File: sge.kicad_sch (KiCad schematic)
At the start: 27 parts, among them IC6 315-5660

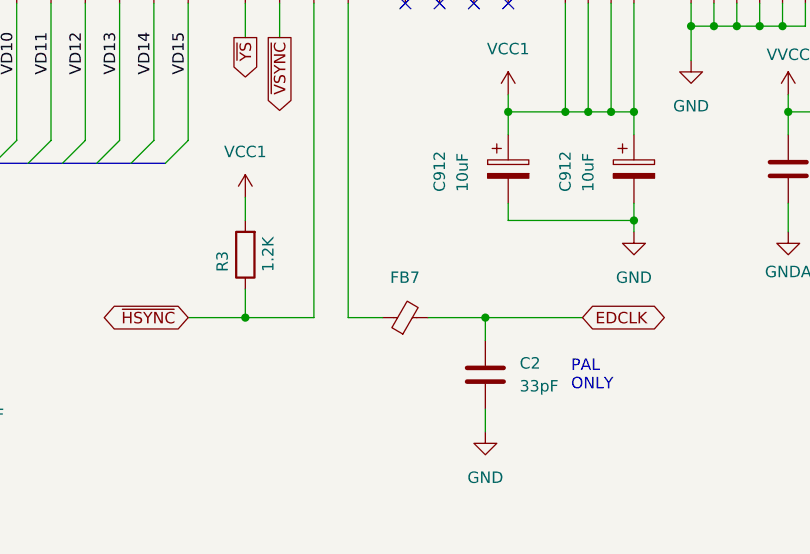
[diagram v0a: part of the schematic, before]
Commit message: Ferrite Bead LCSC Part update
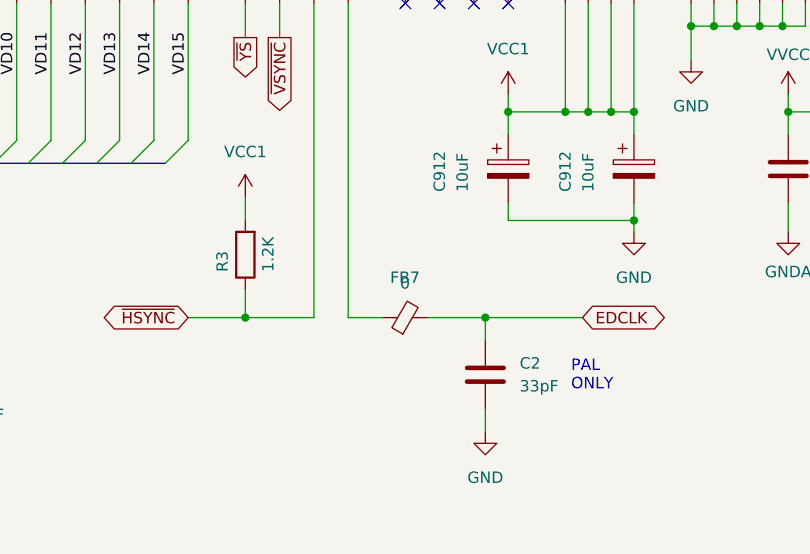
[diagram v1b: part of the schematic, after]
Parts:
- FB7: value ~ -> 0; LCSC Part # C2441367 -> C91037
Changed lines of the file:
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@@
       (effects (font (size 1.27 1.27)))
     )
-    (property "Value" "~" (at 252.6919 250.825 90)
+    (property "Value" "0" (at 252.6919 250.825 90)
       (effects (font (size 1.27 1.27)))
     )
@@
       (effects (font (size 1.27 1.27)) hide)
     )
-    (property "LCSC Part #" "C2441367" (at 252.73 254.635 0)
+    (property "LCSC Part #" "C91037" (at 252.73 254.635 0)
       (effects (font (size 1.27 1.27)) hide)
     )

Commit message: more component parts updated
Full in the * as PAL versions.
Added MPN for PCBWAY
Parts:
- C1: MPN (none) -> VJ0805Y223JXJPW1BC
- C1: MPN (none) -> VJ0805A470FXJPW1BC
- C2: MPN (none) -> VJ0805A330FXJPW1BC
- C8: MPN (none) -> VJ0805Y105KXJTW1BC
- FB7: MPN (none) -> CBG201209U000T
- R3: MPN (none) -> CRCW08052K20JNEA
- R3: MPN (none) -> CRCW08054K70JNEAC
- R3: MPN (none) -> CRCW08051K20FKEAHP
- RA1, RA2, RA3, RA4, RA5: MPN (none) -> YC164-FR-07100RL
- RA6: MPN (none) -> YC162-FR-07100RL
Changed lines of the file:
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@@
+      (effects (font (size 1.27 1.27)) hide)
+    )
+    (property "MPN" "YC164-FR-07100RL" (at 113.03 38.1 0)
       (effects (font (size 1.27 1.27)) hide)
     )
@@
     )
     (property "LCSC Part #" "" (at 213.36 130.81 0)
+      (effects (font (size 1.27 1.27)) hide)
+    )
+    (property "MPN" "" (at 213.36 130.81 0)
       (effects (font (size 1.27 1.27)) hide)
     )
@@
       (effects (font (size 1.27 1.27)) hide)
     )
+    (property "MPN" "CRCW08052K20JNEA" (at 139.7 256.54 0)
+      (effects (font (size 1.27 1.27)) hide)
+    )
     (pin "1")
     (pin "2")
@@
     )
     (property "LCSC Part #" "C136838" (at 99.06 38.1 0)
+      (effects (font (size 1.27 1.27)) hide)
+    )
+    (property "MPN" "YC164-FR-07100RL" (at 99.06 38.1 0)
       (effects (font (size 1.27 1.27)) hide)
     )
@@
       (effects (font (size 1.27 1.27)) hide)
     )
+    (property "MPN" "YC164-FR-07100RL" (at 124.46 38.1 0)
+      (effects (font (size 1.27 1.27)) hide)
+    )
     (pin "1")
     (pin "8")
@@
       (effects (font (size 1.27 1.27)) hide)
     )
+    (property "MPN" "YC164-FR-07100RL" (at 116.84 38.1 0)
+      (effects (font (size 1.27 1.27)) hide)
+    )
     (pin "1")
     (pin "8")
@@
       (effects (font (size 1.27 1.27)) hide)
     )
+    (property "MPN" "" (at 264.16 238.125 0)
+      (effects (font (size 1.27 1.27)) hide)
+    )
     (pin "1")
     (pin "2")
@@
     )
     (property "LCSC Part #" "C136838" (at 198.12 38.1 0)
+      (effects (font (size 1.27 1.27)) hide)
+    )
+    (property "MPN" "YC164-FR-07100RL" (at 198.12 38.1 0)
       (effects (font (size 1.27 1.27)) hide)
     )
@@
       (effects (font (size 1.27 1.27)) hide)
     )
+    (property "MPN" "VJ0805A330FXJPW1BC" (at 261.62 260.985 0)
+      (effects (font (size 1.27 1.27)) hide)
+    )
     (pin "1")
     (pin "2")
@@
       (effects (font (size 1.27 1.27)) hide)
     )
+    (property "MPN" "YC162-FR-07100RL" (at 106.68 38.1 0)
+      (effects (font (size 1.27 1.27)) hide)
+    )
     (pin "1")
     (pin "4")
@@
       (effects (font (size 1.27 1.27)) hide)
     )
+    (property "MPN" "CRCW08052K20JNEA" (at 392.43 52.07 0)
+      (effects (font (size 1.27 1.27)) hide)
+    )
     (pin "1")
     (pin "2")
@@
       (effects (font (size 1.27 1.27)) hide)
     )
+    (property "MPN" "VJ0805Y223JXJPW1BC" (at 175.26 264.16 0)
+      (effects (font (size 1.27 1.27)) hide)
+    )
     (pin "1")
     (pin "2")
@@
       (effects (font (size 1.27 1.27)) hide)
     )
+    (property "MPN" "VJ0805Y105KXJTW1BC" (at 30.48 174.625 0)
+      (effects (font (size 1.27 1.27)) hide)
+    )
     (pin "1")
     (pin "2")
@@
       (effects (font (size 1.27 1.27)) hide)
     )
+    (property "MPN" "VJ0805Y223JXJPW1BC" (at 160.655 264.16 0)
+      (effects (font (size 1.27 1.27)) hide)
+    )
     (pin "1")
     (pin "2")
@@
       (effects (font (size 1.27 1.27)) hide)
     )
+    (property "MPN" "VJ0805Y223JXJPW1BC" (at 295.275 238.125 0)
+      (effects (font (size 1.27 1.27)) hide)
+    )
     (pin "1")
     (pin "2")
@@
     )
     (property "LCSC Part #" "C136838" (at 135.89 38.1 0)
+      (effects (font (size 1.27 1.27)) hide)
+    )
+    (property "MPN" "YC164-FR-07100RL" (at 135.89 38.1 0)
       (effects (font (size 1.27 1.27)) hide)
     )
@@
       (effects (font (size 1.27 1.27)) hide)
     )
+    (property "MPN" "YC162-FR-07100RL" (at 83.82 38.1 0)
+      (effects (font (size 1.27 1.27)) hide)
+    )
     (pin "1")
     (pin "4")
@@
     )
     (property "LCSC Part #" "C136838" (at 120.65 38.1 0)
+      (effects (font (size 1.27 1.27)) hide)
+    )
+    (property "MPN" "YC164-FR-07100RL" (at 120.65 38.1 0)
       (effects (font (size 1.27 1.27)) hide)
     )
@@
       (effects (font (size 1.27 1.27)) hide)
     )
+    (property "MPN" "YC164-FR-07100RL" (at 179.07 38.1 0)
+      (effects (font (size 1.27 1.27)) hide)
+    )
     (pin "1")
     (pin "8")
@@
       (effects (font (size 1.27 1.27)) hide)
     )
+    (property "MPN" "CRCW08052K20JNEA" (at 354.33 229.87 0)
+      (effects (font (size 1.27 1.27)) hide)
+    )
     (pin "1")
     (pin "2")
@@
     )
     (property "LCSC Part #" "C136838" (at 132.08 38.1 0)
+      (effects (font (size 1.27 1.27)) hide)
+    )
+    (property "MPN" "YC164-FR-07100RL" (at 132.08 38.1 0)
       (effects (font (size 1.27 1.27)) hide)
     )
@@
       (effects (font (size 1.27 1.27)) hide)
     )
+    (property "MPN" "" (at 127 256.54 0)
+      (effects (font (size 1.27 1.27)) hide)
+    )
     (pin "1")
     (pin "2")
@@
     )
     (property "LCSC Part #" "C136838" (at 201.93 38.1 0)
+      (effects (font (size 1.27 1.27)) hide)
+    )
+    (property "MPN" "YC164-FR-07100RL" (at 201.93 38.1 0)
       (effects (font (size 1.27 1.27)) hide)
     )
@@
       (effects (font (size 1.27 1.27)) hide)
     )
+    (property "MPN" "VJ0805Y223JXJPW1BC" (at 321.31 238.125 0)
+      (effects (font (size 1.27 1.27)) hide)
+    )
     (pin "1")
     (pin "2")
@@
     )
     (property "LCSC Part #" "C136838" (at 194.31 38.1 0)
+      (effects (font (size 1.27 1.27)) hide)
+    )
+    (property "MPN" "YC164-FR-07100RL" (at 194.31 38.1 0)
       (effects (font (size 1.27 1.27)) hide)
     )
@@
       (effects (font (size 1.27 1.27)) hide)
     )
+    (property "MPN" "YC164-FR-07100RL" (at 128.27 38.1 0)
+      (effects (font (size 1.27 1.27)) hide)
+    )
     (pin "1")
     (pin "8")
@@
       (effects (font (size 1.27 1.27)) hide)
     )
+    (property "MPN" "YC164-FR-07100RL" (at 102.87 38.1 0)
+      (effects (font (size 1.27 1.27)) hide)
+    )
     (pin "1")
     (pin "8")
@@
       (effects (font (size 1.27 1.27)) hide)
     )
+    (property "MPN" "CRCW08054K70JNEAC" (at 390.525 195.58 0)
+      (effects (font (size 1.27 1.27)) hide)
+    )
     (pin "1")
     (pin "2")
@@
       (effects (font (size 1.27 1.27)) hide)
     )
+    (property "MPN" "VJ0805Y223JXJPW1BC" (at 314.96 238.125 0)
+      (effects (font (size 1.27 1.27)) hide)
+    )
     (pin "1")
     (pin "2")
@@
     )
     (property "LCSC Part #" "C136838" (at 80.01 38.1 0)
+      (effects (font (size 1.27 1.27)) hide)
+    )
+    (property "MPN" "YC164-FR-07100RL" (at 80.01 38.1 0)
       (effects (font (size 1.27 1.27)) hide)
     )
@@
       (effects (font (size 1.27 1.27)) hide)
     )
+    (property "MPN" "CBG201209U000T" (at 252.73 254.635 0)
+      (effects (font (size 1.27 1.27)) hide)
+    )
     (pin "1")
     (pin "2")
@@
     )
     (property "LCSC Part #" "C136838" (at 190.5 38.1 0)
+      (effects (font (size 1.27 1.27)) hide)
+    )
+    (property "MPN" "YC164-FR-07100RL" (at 190.5 38.1 0)
       (effects (font (size 1.27 1.27)) hide)
     )
@@
       (effects (font (size 1.27 1.27)) hide)
     )
+    (property "MPN" "YC164-FR-07100RL" (at 139.7 38.1 0)
+      (effects (font (size 1.27 1.27)) hide)
+    )
     (pin "1")
     (pin "8")
@@
       (effects (font (size 1.27 1.27)) hide)
     )
+    (property "MPN" "CRCW08051K20FKEAHP" (at 234.95 247.65 0)
+      (effects (font (size 1.27 1.27)) hide)
+    )
     (pin "1")
     (pin "2")
@@
       (effects (font (size 1.27 1.27)) hide)
     )
+    (property "MPN" "" (at 278.13 238.125 0)
+      (effects (font (size 1.27 1.27)) hide)
+    )
     (pin "1")
     (pin "2")
@@
     )
     (property "LCSC Part #" "C136838" (at 205.74 38.1 0)
+      (effects (font (size 1.27 1.27)) hide)
+    )
+    (property "MPN" "YC164-FR-07100RL" (at 205.74 38.1 0)
       (effects (font (size 1.27 1.27)) hide)
     )
@@
       (effects (font (size 1.27 1.27)) hide)
     )
+    (property "MPN" "VJ0805A470FXJPW1BC" (at 388.62 72.39 0)
+      (effects (font (size 1.27 1.27)) hide)
+    )
     (pin "1")
     (pin "2")
@@
     )
     (property "LCSC Part #" "C136838" (at 95.25 38.1 0)
+      (effects (font (size 1.27 1.27)) hide)
+    )
+    (property "MPN" "YC164-FR-07100RL" (at 95.25 38.1 0)
       (effects (font (size 1.27 1.27)) hide)
     )
@@
       (effects (font (size 1.27 1.27)) hide)
     )
+    (property "MPN" "VJ0805Y105KXJTW1BC" (at 31.115 71.755 0)
+      (effects (font (size 1.27 1.27)) hide)
+    )
     (pin "1")
     (pin "2")
@@
       (effects (font (size 1.27 1.27)) hide)
     )
+    (property "MPN" "VJ0805Y223JXJPW1BC" (at 200.025 264.16 0)
+      (effects (font (size 1.27 1.27)) hide)
+    )
     (pin "1")
     (pin "2")
@@
     )
     (property "LCSC Part #" "C136838" (at 186.69 38.1 0)
+      (effects (font (size 1.27 1.27)) hide)
+    )
+    (property "MPN" "YC164-FR-07100RL" (at 186.69 38.1 0)
       (effects (font (size 1.27 1.27)) hide)
     )
@@
       (effects (font (size 1.27 1.27)) hide)
     )
+    (property "MPN" "VJ0805Y223JXJPW1BC" (at 187.96 264.16 0)
+      (effects (font (size 1.27 1.27)) hide)
+    )
     (pin "1")
     (pin "2")
@@
       (effects (font (size 1.27 1.27)) hide)
     )
+    (property "MPN" "YC164-FR-07100RL" (at 182.88 38.1 0)
+      (effects (font (size 1.27 1.27)) hide)
+    )

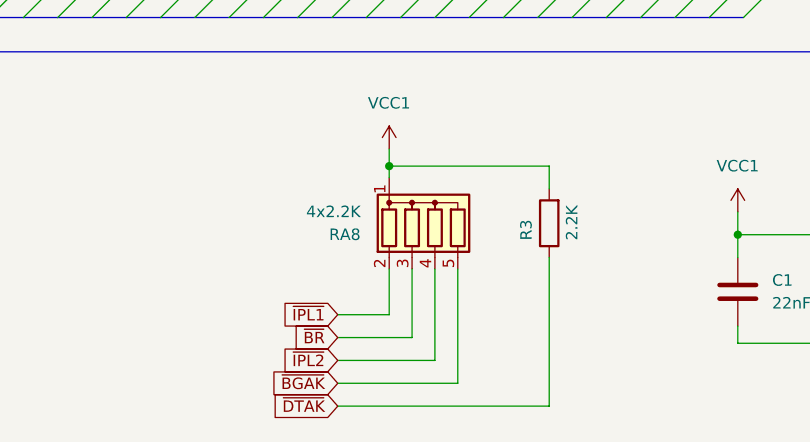
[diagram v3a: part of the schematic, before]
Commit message: Use more readily-available resistor packs.
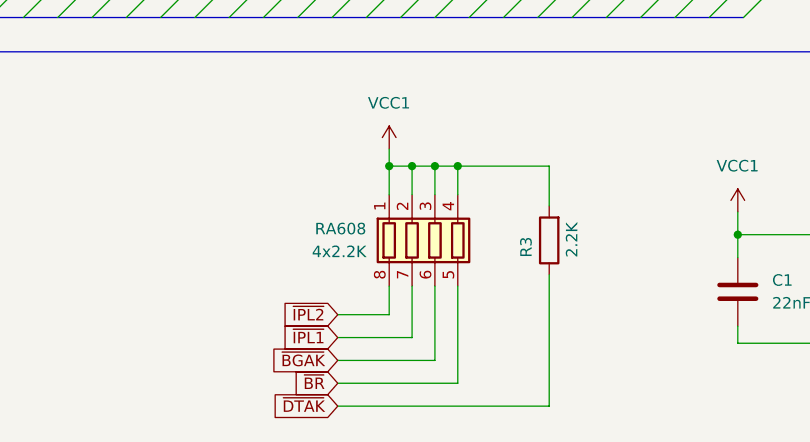
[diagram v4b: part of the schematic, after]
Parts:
- removed RA8: 4x2.2K, Neptune:RA_4_Common, symbol Device:R_Network04
- added RA608: 4x2.2K, Resistor_SMD:R_Array_Convex_4x0603, symbol Device:R_Pack04
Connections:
- net VCC1: now also RA608.1 (R1.1), RA608.2 (R2.1), RA608.3 (R3.1), RA608.4 (R4.1)
- net ~{BGAK}: now also RA608.6 (R3.2)
- net ~{BR}: now also RA608.5 (R4.2)
- net ~{IPL1}: now also RA608.7 (R2.2)
- net ~{IPL2}: now also RA608.8 (R1.2)
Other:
- moved on the sheet: R3
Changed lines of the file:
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@@
   (junction (at 292.1 222.25) (diameter 0) (color 0 0 0 0)
   )
+  (junction (at 127 250.19) (diameter 0) (color 0 0 0 0)
+  )
   (junction (at 388.62 60.96) (diameter 0) (color 0 0 0 0)
   )
@@
   (junction (at 31.115 64.77) (diameter 0) (color 0 0 0 0)
   )
+  (junction (at 129.54 250.19) (diameter 0) (color 0 0 0 0)
+  )
   (junction (at 278.13 243.84) (diameter 0) (color 0 0 0 0)
   )
@@
   (junction (at 234.95 254.635) (diameter 0) (color 0 0 0 0)
   )
+  (junction (at 124.46 250.19) (diameter 0) (color 0 0 0 0)
+  )
   (junction (at 289.56 222.25) (diameter 0) (color 0 0 0 0)
   )
@@
     (stroke (width 0) (type default))
   )
-  (wire (pts (xy 124.46 269.24) (xy 124.46 261.62))
+  (wire (pts (xy 124.46 269.24) (xy 124.46 263.525))
     (stroke (width 0) (type default))
   )
@@
     (stroke (width 0) (type default))
   )
+  (wire (pts (xy 129.54 250.19) (xy 129.54 253.365))
+    (stroke (width 0) (type default))
+  )
   (wire (pts (xy 314.96 243.84) (xy 321.31 243.84))
     (stroke (width 0) (type default))
@@
     (stroke (width 0) (type default))
   )
-  (wire (pts (xy 121.92 250.19) (xy 139.7 250.19))
+  (wire (pts (xy 121.92 250.19) (xy 124.46 250.19))
     (stroke (width 0) (type default))
   )
@@
     (stroke (width 0) (type default))
   )
+  (wire (pts (xy 127 250.19) (xy 127 253.365))
+    (stroke (width 0) (type default))
+  )
   (bus (pts (xy 299.72 24.13) (xy 295.91 24.13))
     (stroke (width 0) (type default))
@@
     (stroke (width 0) (type default))
   )
+  (wire (pts (xy 127 250.19) (xy 129.54 250.19))
+    (stroke (width 0) (type default))
+  )
   (bus (pts (xy 153.67 233.68) (xy 157.48 233.68))
     (stroke (width 0) (type default))
@@
     (stroke (width 0) (type default))
   )
-  (wire (pts (xy 121.92 250.19) (xy 121.92 251.46))
+  (wire (pts (xy 121.92 250.19) (xy 121.92 253.365))
     (stroke (width 0) (type default))
   )
@@
     (stroke (width 0) (type default))
   )
+  (wire (pts (xy 124.46 250.19) (xy 127 250.19))
+    (stroke (width 0) (type default))
+  )
   (wire (pts (xy 113.03 22.86) (xy 113.03 34.29))
     (stroke (width 0) (type default))
@@
     (stroke (width 0) (type default))
   )
-  (wire (pts (xy 129.54 274.32) (xy 129.54 261.62))
+  (wire (pts (xy 129.54 274.32) (xy 129.54 263.525))
     (stroke (width 0) (type default))
   )
@@
     (stroke (width 0) (type default))
   )
+  (wire (pts (xy 129.54 250.19) (xy 139.7 250.19))
+    (stroke (width 0) (type default))
+  )
   (wire (pts (xy 364.49 156.21) (xy 375.92 156.21))
     (stroke (width 0) (type default))
@@
     (stroke (width 0) (type default))
   )
+  (wire (pts (xy 124.46 250.19) (xy 124.46 253.365))
+    (stroke (width 0) (type default))
+  )
   (wire (pts (xy 50.8 129.54) (xy 62.23 129.54))
     (stroke (width 0) (type default))
@@
     (stroke (width 0) (type default))
   )
-  (wire (pts (xy 121.92 266.7) (xy 121.92 261.62))
+  (wire (pts (xy 121.92 266.7) (xy 121.92 263.525))
     (stroke (width 0) (type default))
   )
@@
     (stroke (width 0) (type default))
   )
-  (wire (pts (xy 127 271.78) (xy 127 261.62))
+  (wire (pts (xy 127 271.78) (xy 127 263.525))
     (stroke (width 0) (type default))
   )
@@
     (stroke (width 0) (type default))
   )
-  (wire (pts (xy 139.7 250.19) (xy 139.7 252.73))
+  (wire (pts (xy 139.7 250.19) (xy 139.7 254.635))
     (stroke (width 0) (type default))
   )
@@
     (stroke (width 0) (type default))
   )
-  (wire (pts (xy 139.7 276.86) (xy 139.7 260.35))
+  (wire (pts (xy 139.7 276.86) (xy 139.7 262.255))
     (stroke (width 0) (type default))
   )
@@
     )
   )
-  (global_label "~{IPL2}" (shape input) (at 116.205 271.78 180) (fields_autoplaced)
+  (global_label "~{IPL2}" (shape input) (at 116.205 266.7 180) (fields_autoplaced)
     (effects (font (size 1.27 1.27)) (justify right))
-    (property "Intersheetrefs" "${INTERSHEET_REFS}" (at 109.1074 271.78 0)
+    (property "Intersheetrefs" "${INTERSHEET_REFS}" (at 109.1074 266.7 0)
       (effects (font (size 1.27 1.27)) (justify right) hide)
     )
@@
     )
   )
-  (global_label "~{IPL1}" (shape input) (at 116.205 266.7 180) (fields_autoplaced)
+  (global_label "~{IPL1}" (shape input) (at 116.205 269.24 180) (fields_autoplaced)
     (effects (font (size 1.27 1.27)) (justify right))
-    (property "Intersheetrefs" "${INTERSHEET_REFS}" (at 109.1074 266.7 0)
+    (property "Intersheetrefs" "${INTERSHEET_REFS}" (at 109.1074 269.24 0)
       (effects (font (size 1.27 1.27)) (justify right) hide)
     )
@@
     )
   )
-  (global_label "~{BGAK}" (shape input) (at 116.205 274.32 180) (fields_autoplaced)
+  (global_label "~{BGAK}" (shape input) (at 116.205 271.78 180) (fields_autoplaced)
     (effects (font (size 1.27 1.27)) (justify right))
-    (property "Intersheetrefs" "${INTERSHEET_REFS}" (at 108.3212 274.32 0)
+    (property "Intersheetrefs" "${INTERSHEET_REFS}" (at 108.3212 271.78 0)
       (effects (font (size 1.27 1.27)) (justify right) hide)
     )
@@
     )
   )
-  (global_label "~{BR}" (shape input) (at 116.205 269.24 180) (fields_autoplaced)
+  (global_label "~{BR}" (shape input) (at 116.205 274.32 180) (fields_autoplaced)
     (effects (font (size 1.27 1.27)) (justify right))
-    (property "Intersheetrefs" "${INTERSHEET_REFS}" (at 110.6798 269.24 0)
+    (property "Intersheetrefs" "${INTERSHEET_REFS}" (at 110.6798 274.32 0)
       (effects (font (size 1.27 1.27)) (justify right) hide)
     )
@@
     )
   )
-  (symbol (lib_id "Device:R") (at 139.7 256.54 180) (unit 1)
+  (symbol (lib_id "Device:R") (at 139.7 258.445 180) (unit 1)
     (in_bom yes) (on_board yes) (dnp no)
-    (property "Reference" "R3" (at 137.16 258.445 90)
+    (property "Reference" "R3" (at 137.16 260.35 90)
       (effects (font (size 1.27 1.27)) (justify right))
     )
-    (property "Value" "2.2K" (at 142.24 258.445 90)
+    (property "Value" "2.2K" (at 142.24 260.35 90)
       (effects (font (size 1.27 1.27)) (justify right))
     )
-    (property "Footprint" "Resistor_SMD:R_0805_2012Metric" (at 141.478 256.54 90)
+    (property "Footprint" "Resistor_SMD:R_0805_2012Metric" (at 141.478 258.445 90)
       (effects (font (size 1.27 1.27)) hide)
     )
-    (property "Datasheet" "~" (at 139.7 256.54 0)
+    (property "Datasheet" "~" (at 139.7 258.445 0)
       (effects (font (size 1.27 1.27)) hide)
     )
-    (property "DigiKey" "P2.20KCCT-ND" (at 139.7 256.54 0)
+    (property "DigiKey" "P2.20KCCT-ND" (at 139.7 258.445 0)
       (effects (font (size 1.27 1.27)) hide)
     )
-    (property "LCSC Part #" "C3008897" (at 139.7 256.54 0)
+    (property "LCSC Part #" "C3008897" (at 139.7 258.445 0)
       (effects (font (size 1.27 1.27)) hide)
     )
-    (property "MPN" "CRCW08052K20JNEA" (at 139.7 256.54 0)
+    (property "MPN" "CRCW08052K20JNEA" (at 139.7 258.445 0)
       (effects (font (size 1.27 1.27)) hide)
     )
@@
     )
   )
-  (symbol (lib_id "Device:R_Network04") (at 127 256.54 0) (unit 1)
-    (in_bom yes) (on_board yes) (dnp no)
-    (property "Reference" "RA8" (at 118.745 257.81 0)
-      (effects (font (size 1.27 1.27)) (justify right))
-    )
-    (property "Value" "4x2.2K" (at 118.745 255.27 0)
-      (effects (font (size 1.27 1.27)) (justify right))
-    )
-    (property "Footprint" "Neptune:RA_4_Common" (at 133.985 256.54 90)
-      (effects (font (size 1.27 1.27)) hide)
-    )
-    (property "Datasheet" "http://www.vishay.com/docs/31509/csc.pdf" (at 127 256.54 0)
-      (effects (font (size 1.27 1.27)) hide)
-    )
-    (property "DigiKey" "" (at 127 256.54 0)
-      (effects (font (size 1.27 1.27)) hide)
-    )
-    (property "LCSC Part #" "" (at 127 256.54 0)
-      (effects (font (size 1.27 1.27)) hide)
-    )
-    (property "MPN" "" (at 127 256.54 0)
-      (effects (font (size 1.27 1.27)) hide)
-    )
-    (pin "1")
-    (pin "2")
-    (pin "3")
-    (pin "4")
-    (pin "5")
-    (instances
-      (project "Neptune"
-        (path "/bcc23b51-b742-4ae5-9dd6-d96a24058944/0d895458-d3d0-4635-bde5-e15500822f5f"
-          (reference "RA8") (unit 1)
-        )
-      )
-    )
-  )
   (symbol (lib_id "power:GND") (at 31.115 78.105 0) (unit 1)
     (in_bom yes) (on_board yes) (dnp no) (fields_autoplaced)
@@
         )
       )
+    )
+  )
+  (symbol (lib_id "Device:R_Pack04") (at 127 258.445 0) (mirror x) (unit 1)
+    (in_bom yes) (on_board yes) (dnp no) (fields_autoplaced)
+    (property "Reference" "RA608" (at 119.38 257.175 0)
+      (effects (font (size 1.27 1.27)) (justify right))
+    )
+    (property "Value" "4x2.2K" (at 119.38 259.715 0)
+      (effects (font (size 1.27 1.27)) (justify right))
+    )
+    (property "Footprint" "Resistor_SMD:R_Array_Convex_4x0603" (at 133.985 258.445 90)
+      (effects (font (size 1.27 1.27)) hide)
+    )
+    (property "Datasheet" "~" (at 127 258.445 0)
+      (effects (font (size 1.27 1.27)) hide)
+    )
+    (pin "1")
+    (pin "2")
+    (pin "3")
+    (pin "4")
+    (pin "5")
+    (pin "6")
+    (pin "7")
+    (pin "8")
+    (instances
+      (project "Neptune"
+        (path "/bcc23b51-b742-4ae5-9dd6-d96a24058944/0d895458-d3d0-4635-bde5-e15500822f5f"
+          (reference "RA608") (unit 1)
+        )
+      )
